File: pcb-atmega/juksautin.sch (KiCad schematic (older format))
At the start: 29 parts, among them J1 Screw_Terminal_01x09, J3 USB_C_Receptacle_USB2.0, J4 TagConnect, U1 SP3485EN, U2 SRV05-4, U3 LM2576S-5, U4 ATmega32U4-AU, Y1 X322516MLB4SI

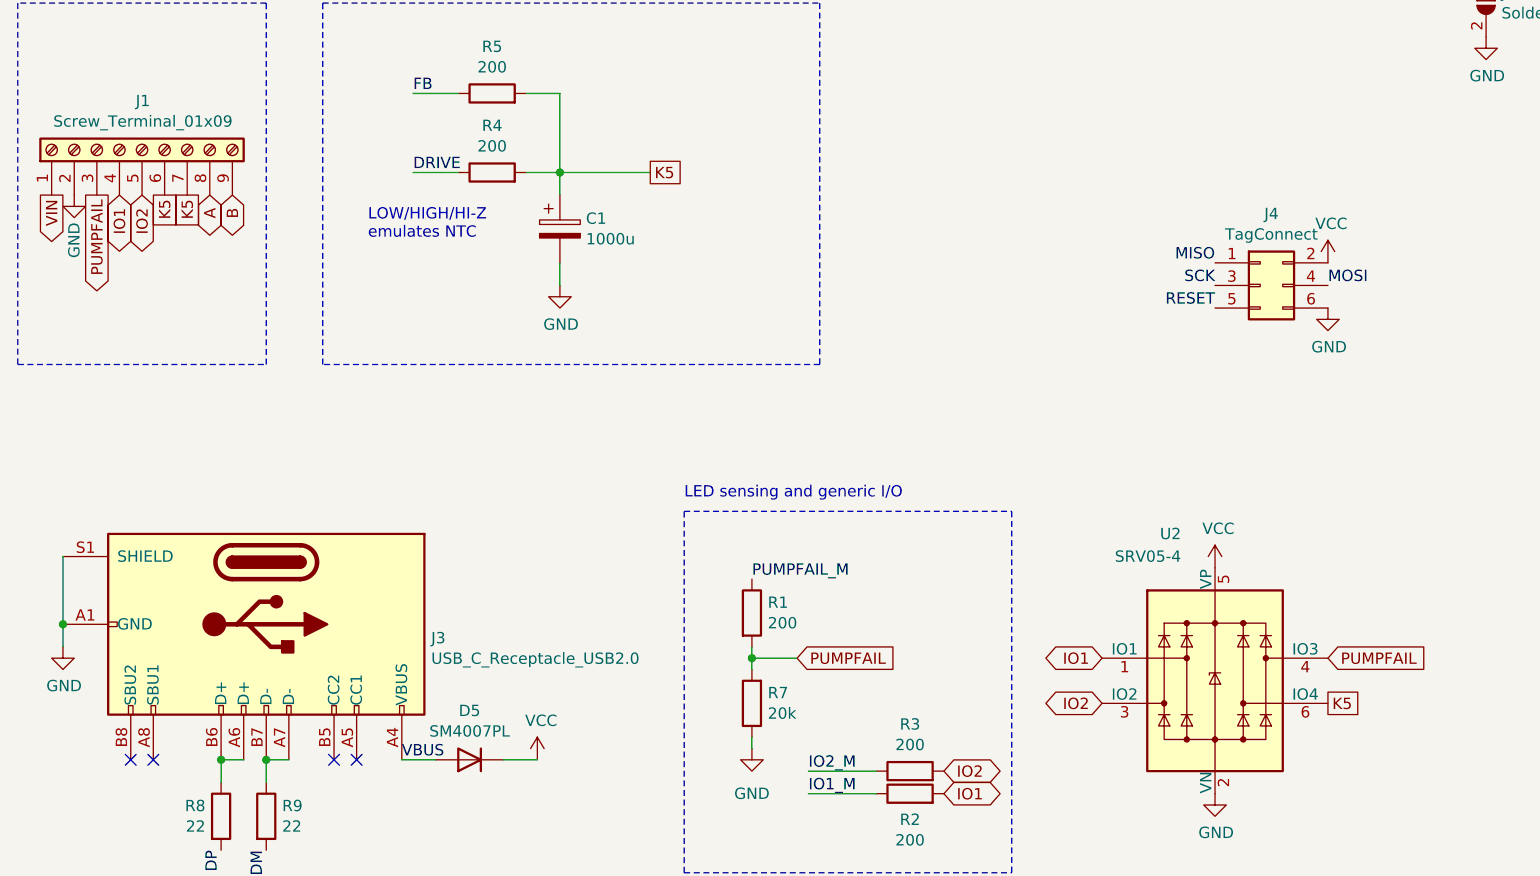
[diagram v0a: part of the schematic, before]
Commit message: pcb: Rename K5 to K9 everywhere
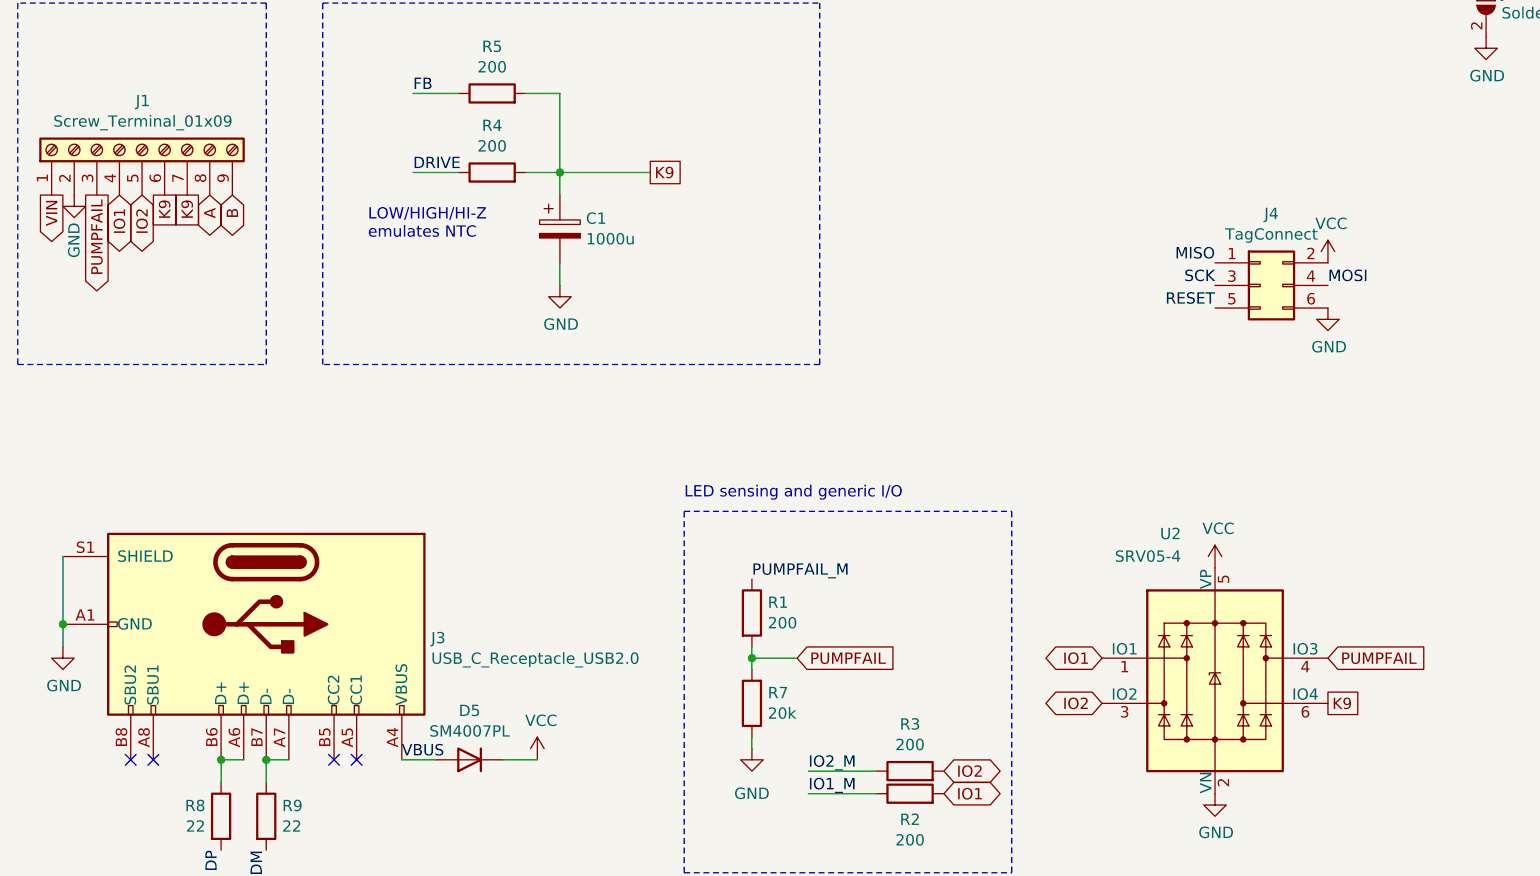
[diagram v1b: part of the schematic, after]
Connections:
- net labels added: K9
- net labels removed: K5
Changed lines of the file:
@@
 $EndComp
 Text GLabel 3650 3800 2    50   UnSpc ~ 0
-K5
+K9
 $Comp
 L Device:R R4
@@
 B
 Text GLabel 1600 3900 3    50   UnSpc ~ 0
-K5
+K9
 Text GLabel 1500 3900 3    50   UnSpc ~ 0
-K5
+K9
 Text GLabel 5150 1750 2    50   3State ~ 0
 A
@@
 PUMPFAIL
 Text GLabel 6650 6150 2    50   UnSpc ~ 0
-K5
+K9
 $Comp
 L power:GND #PWR011

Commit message: pcb: Route everything Atmega board
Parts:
- removed TP1: AR, TestPoint:TestPoint_Pad_D1.0mm, symbol Connector:TestPoint
- added J2: Power out, Connector_PinHeader_2.54mm:PinHeader_1x02_P2.54mm_Vertical, symbol Connector:Conn_01x02_Male
- added J5: Conn_01x03, Connector_PinHeader_2.54mm:PinHeader_1x03_P2.54mm_Vertical, symbol Connector_Generic:Conn_01x03
- added J6: AREF_OUT, Connector_PinHeader_2.54mm:PinHeader_1x02_P2.54mm_Vertical, symbol Connector_Generic:Conn_01x02
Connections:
- wire segments 71 -> 79
- no-connect marks 19 -> 16
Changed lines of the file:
@@
 Wire Wire Line
 	9450 1000 9450 1100
-Wire Wire Line
-	9450 1100 9550 1100
-Connection ~ 9550 1100
-Wire Wire Line
-	9550 1100 9650 1100
 Text Label 8950 2000 2    50   ~ 0
 AREF
@@
 Text GLabel 5650 6150 0    50   3State ~ 0
 IO2
-Text GLabel 6650 5950 2    50   Input ~ 0
+Text GLabel 6650 6150 2    50   Input ~ 0
 PUMPFAIL
-Text GLabel 6650 6150 2    50   UnSpc ~ 0
+Text GLabel 6650 5950 2    50   UnSpc ~ 0
 K9
 $Comp
@@
 Wire Wire Line
 	4100 6300 4100 6350
-Connection ~ 9450 4700
-Connection ~ 9450 1100
-$Comp
-L MCU_Microchip_ATmega:ATmega32U4-AU U4
-U 1 1 60B53808
-P 9550 2900
-F 0 "U4" H 9550 1011 50  0000 L CNN
-F 1 "ATmega32U4-AU" H 9550 920 50  0000 L CNN
-F 2 "Package_QFP:TQFP-44_10x10mm_P0.8mm" H 9550 2900 50  0001 C CIN
-F 3 "http://ww1.microchip.com/downloads/en/DeviceDoc/Atmel-7766-8-bit-AVR-ATmega16U4-32U4_Datasheet.pdf" H 9550 2900 50  0001 C CNN
-F 4 "C44854" H 9550 2900 50  0001 C CNN "LCSC"
-	1    9550 2900
-	1    0    0    -1
-$EndComp
 Text GLabel 4950 6450 2    50   3State ~ 0
 IO2
@@
 NoConn ~ 10150 2400
 NoConn ~ 10150 2600
-NoConn ~ 10150 3000
-NoConn ~ 10150 3100
-NoConn ~ 10150 3200
-NoConn ~ 10150 3300
 NoConn ~ 10150 3500
 NoConn ~ 10150 3600
 NoConn ~ 10150 3800
 NoConn ~ 10150 3900
-Connection ~ 8400 2000
-$Comp
-L Connector:TestPoint TP1
-U 1 1 60EAECA1
-P 8400 2000
-F 0 "TP1" V 8446 2188 50  0000 L CNN
-F 1 "AR" V 8355 2188 50  0000 L CNN
-F 2 "TestPoint:TestPoint_Pad_D1.0mm" H 8600 2000 50  0001 C CNN
-F 3 "~" H 8600 2000 50  0001 C CNN
-	1    8400 2000
-	0    -1   -1   0
-$EndComp
 Text Label 8950 1400 2    50   ~ 0
 RESET
@@
 	1    0    0    -1
 $EndComp
+$Comp
+L power:GND #PWR0106
+U 1 1 60C3103F
+P 5800 3500
+F 0 "#PWR0106" H 5800 3250 50  0001 C CNN
+F 1 "GND" H 5950 3500 50  0000 C CNN
+F 2 "" H 5800 3500 50  0001 C CNN
+F 3 "" H 5800 3500 50  0001 C CNN
+	1    5800 3500
+	1    0    0    -1
+$EndComp
+$Comp
+L power:VCC #PWR0110
+U 1 1 60C31968
+P 5800 3400
+F 0 "#PWR0110" H 5800 3250 50  0001 C CNN
+F 1 "VCC" H 5950 3400 50  0000 C CNN
+F 2 "" H 5800 3400 50  0001 C CNN
+F 3 "" H 5800 3400 50  0001 C CNN
+	1    5800 3400
+	1    0    0    -1
+$EndComp
+$Comp
+L Connector:Conn_01x02_Male J2
+U 1 1 60C5E35B
+P 5600 3400
+F 0 "J2" H 5708 3581 50  0000 R CNN
+F 1 "Power out" H 5708 3490 50  0000 R CNN
+F 2 "Connector_PinHeader_2.54mm:PinHeader_1x02_P2.54mm_Vertical" H 5600 3400 50  0001 C CNN
+F 3 "~" H 5600 3400 50  0001 C CNN
+	1    5600 3400
+	1    0    0    -1
+$EndComp
+Connection ~ 9450 4700
+Connection ~ 9450 1100
+Wire Wire Line
+	9550 1100 9650 1100
+Wire Wire Line
+	9450 1100 9550 1100
+Connection ~ 9550 1100
+$Comp
+L MCU_Microchip_ATmega:ATmega32U4-AU U4
+U 1 1 60B53808
+P 9550 2900
+F 0 "U4" H 9550 1011 50  0000 L CNN
+F 1 "ATmega32U4-AU" H 9550 920 50  0000 L CNN
+F 2 "Package_QFP:TQFP-44_10x10mm_P0.8mm" H 9550 2900 50  0001 C CIN
+F 3 "http://ww1.microchip.com/downloads/en/DeviceDoc/Atmel-7766-8-bit-AVR-ATmega16U4-32U4_Datasheet.pdf" H 9550 2900 50  0001 C CNN
+F 4 "C44854" H 9550 2900 50  0001 C CNN "LCSC"
+	1    9550 2900
+	1    0    0    -1
+$EndComp
+$Comp
+L Connector_Generic:Conn_01x03 J5
+U 1 1 60C825FD
+P 10500 3200
+F 0 "J5" H 10580 3242 50  0000 L CNN
+F 1 "Conn_01x03" H 10580 3151 50  0000 L CNN
+F 2 "Connector_PinHeader_2.54mm:PinHeader_1x03_P2.54mm_Vertical" H 10500 3200 50  0001 C CNN
+F 3 "~" H 10500 3200 50  0001 C CNN
+	1    10500 3200
+	1    0    0    -1
+$EndComp
+NoConn ~ 10150 3100
+Wire Wire Line
+	10300 3300 10150 3300
+Wire Wire Line
+	10150 3200 10300 3200
+Wire Wire Line
+	10150 3000 10300 3000
+Wire Wire Line
+	10300 3000 10300 3100
+$Comp
+L Connector_Generic:Conn_01x02 J6
+U 1 1 60CB591E
+P 7900 2150
+F 0 "J6" H 7818 2367 50  0000 C CNN
+F 1 "AREF_OUT" H 7818 2276 50  0000 C CNN
+F 2 "Connector_PinHeader_2.54mm:PinHeader_1x02_P2.54mm_Vertical" H 7900 2150 50  0001 C CNN
+F 3 "~" H 7900 2150 50  0001 C CNN
+	1    7900 2150
+	-1   0    0    -1
+$EndComp
+Wire Wire Line
+	8100 2250 8400 2250
+Connection ~ 8400 2250
+Wire Wire Line
+	8100 2150 8250 2150
+Wire Wire Line
+	8250 2150 8250 2000
+Wire Wire Line
+	8250 2000 8400 2000
+Connection ~ 8400 2000
 $EndSCHEMATC

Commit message: pcb: Make schema a bit more readable
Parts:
- J5: value Conn_01x03 -> EXTRA
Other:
- moved on the sheet: C2, C3
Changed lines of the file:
@@
 L power:GND #PWR0109
 U 1 1 60A206FA
-P 2100 2250
-F 0 "#PWR0109" H 2100 2000 50  0001 C CNN
-F 1 "GND" H 2105 2077 50  0000 C CNN
-F 2 "" H 2100 2250 50  0001 C CNN
-F 3 "" H 2100 2250 50  0001 C CNN
-	1    2100 2250
+P 2100 2300
+F 0 "#PWR0109" H 2100 2050 50  0001 C CNN
+F 1 "GND" H 2105 2127 50  0000 C CNN
+F 2 "" H 2100 2300 50  0001 C CNN
+F 3 "" H 2100 2300 50  0001 C CNN
+	1    2100 2300
 	1    0    0    -1
 $EndComp
@@
 Text GLabel 1000 3900 3    50   Output ~ 0
 VIN
-Text GLabel 1150 1650 0    50   Input ~ 0
+Text GLabel 1150 1600 0    50   Input ~ 0
 VIN
 Text Notes 3800 5250 0    50   ~ 0
@@
 	1    0    0    -1
 $EndComp
-Text Label 4250 1650 0    50   ~ 0
+Text Label 4050 1650 0    50   ~ 0
 RX
 Wire Wire Line
-	4250 1650 4350 1650
-Text Label 4250 2050 0    50   ~ 0
+	4050 1650 4350 1650
+Text Label 4050 2050 0    50   ~ 0
 TX
 Wire Wire Line
-	4250 2050 4350 2050
+	4050 2050 4350 2050
 Text Label 10150 2800 0    50   ~ 0
 RX
@@
 L Regulator_Switching:LM2576S-5 U3
 U 1 1 60F0FB4A
-P 2100 1750
-F 0 "U3" H 2100 2117 50  0000 C CNN
-F 1 "LM2576S-5" H 2100 2026 50  0000 C CNN
-F 2 "Package_TO_SOT_SMD:TO-263-5_TabPin3" H 2100 1500 50  0001 L CIN
-F 3 "http://www.ti.com/lit/ds/symlink/lm2576.pdf" H 2100 1750 50  0001 C CNN
-F 4 "C10002" H 2100 1750 50  0001 C CNN "LCSC"
-	1    2100 1750
+P 2100 1700
+F 0 "U3" H 2100 2067 50  0000 C CNN
+F 1 "LM2576S-5" H 2100 1976 50  0000 C CNN
+F 2 "Package_TO_SOT_SMD:TO-263-5_TabPin3" H 2100 1450 50  0001 L CIN
+F 3 "http://www.ti.com/lit/ds/symlink/lm2576.pdf" H 2100 1700 50  0001 C CNN
+F 4 "C10002" H 2100 1700 50  0001 C CNN "LCSC"
+	1    2100 1700
 	1    0    0    -1
 $EndComp
@@
 $EndComp
 Wire Wire Line
-	1250 2250 1250 2050
-Wire Wire Line
-	1600 1850 1600 2250
-Wire Wire Line
-	1600 2250 1250 2250
-Wire Wire Line
-	1600 2250 2100 2250
-Connection ~ 1600 2250
-Wire Wire Line
-	2100 2050 2100 2250
-Connection ~ 2100 2250
-Wire Wire Line
-	2100 2250 2650 2250
-Wire Wire Line
-	3150 1600 3150 1850
+	1250 2300 1250 2100
+Wire Wire Line
+	1600 2300 1250 2300
+Wire Wire Line
+	1600 2300 2100 2300
+Connection ~ 1600 2300
+Connection ~ 2100 2300
+Wire Wire Line
+	3150 1600 3150 1900
 Connection ~ 3150 1600
 $Comp
 L Device:L L1
 U 1 1 60F8C9F3
-P 2900 1850
-F 0 "L1" V 3090 1850 50  0000 C CNN
-F 1 "100uH" V 2999 1850 50  0000 C CNN
-F 2 "Inductor_SMD:L_0805_2012Metric" H 2900 1850 50  0001 C CNN
-F 3 "~" H 2900 1850 50  0001 C CNN
-F 4 "C68035" V 2900 1850 50  0001 C CNN "LCSC"
-	1    2900 1850
+P 2900 1900
+F 0 "L1" V 3090 1900 50  0000 C CNN
+F 1 "100uH" V 2999 1900 50  0000 C CNN
+F 2 "Inductor_SMD:L_0805_2012Metric" H 2900 1900 50  0001 C CNN
+F 3 "~" H 2900 1900 50  0001 C CNN
+F 4 "C68035" V 2900 1900 50  0001 C CNN "LCSC"
+	1    2900 1900
 	0    -1   -1   0
 $EndComp
-Wire Wire Line
-	3050 1850 3150 1850
 $Comp
 L Diode:1N5822 D1
 U 1 1 60F94C7F
-P 2650 2050
-F 0 "D1" V 2604 2130 50  0000 L CNN
-F 1 "SS34" V 2695 2130 50  0000 L CNN
-F 2 "Diode_SMD:D_SMA" H 2650 1875 50  0001 C CNN
-F 3 "http://www.vishay.com/docs/88526/1n5820.pdf" H 2650 2050 50  0001 C CNN
-F 4 "C8678" V 2650 2050 50  0001 C CNN "LCSC"
-	1    2650 2050
+P 2650 2100
+F 0 "D1" V 2604 2180 50  0000 L CNN
+F 1 "SS34" V 2695 2180 50  0000 L CNN
+F 2 "Diode_SMD:D_SMA" H 2650 1925 50  0001 C CNN
+F 3 "http://www.vishay.com/docs/88526/1n5820.pdf" H 2650 2100 50  0001 C CNN
+F 4 "C8678" V 2650 2100 50  0001 C CNN "LCSC"
+	1    2650 2100
 	0    1    1    0
 $EndComp
 Wire Wire Line
-	1150 1650 1250 1650
+	1150 1600 1250 1600
 $Comp
 L Device:CP C2
 U 1 1 60F96B50
-P 1250 1900
-F 0 "C2" H 1368 1946 50  0000 L CNN
-F 1 "100u" H 1368 1855 50  0000 L CNN
-F 2 "Capacitor_SMD:CP_Elec_6.3x7.7" H 1288 1750 50  0001 C CNN
-F 3 "~" H 1250 1900 50  0001 C CNN
-F 4 "C99837" H 1250 1900 50  0001 C CNN "LCSC"
-	1    1250 1900
-	1    0    0    -1
-$EndComp
-Wire Wire Line
-	1250 1750 1250 1650
-Connection ~ 1250 1650
-Wire Wire Line
-	1250 1650 1600 1650
-Wire Wire Line
-	2600 1650 2600 1600
+P 1250 1950
+F 0 "C2" H 1368 1996 50  0000 L CNN
+F 1 "100u" H 1368 1905 50  0000 L CNN
+F 2 "Capacitor_SMD:CP_Elec_6.3x7.7" H 1288 1800 50  0001 C CNN
+F 3 "~" H 1250 1950 50  0001 C CNN
+F 4 "C99837" H 1250 1950 50  0001 C CNN "LCSC"
+	1    1250 1950
+	1    0    0    -1
+$EndComp
+Wire Wire Line
+	1250 1800 1250 1600
+Connection ~ 1250 1600
+Wire Wire Line
+	1250 1600 1600 1600
 Wire Notes Line
 	850  1000 3650 1000
 Wire Notes Line
 	3650 1000 3650 2600
-Connection ~ 3150 1850
 $Comp
 L Device:CP C3
 U 1 1 60F97AAC
-P 3150 2050
-F 0 "C3" H 3268 2096 50  0000 L CNN
-F 1 "1000u" H 3268 2005 50  0000 L CNN
-F 2 "Capacitor_SMD:CP_Elec_8x10" H 3188 1900 50  0001 C CNN
-F 3 "~" H 3150 2050 50  0001 C CNN
-F 4 "C134755" H 3150 2050 50  0001 C CNN "LCSC"
-	1    3150 2050
-	1    0    0    -1
-$EndComp
-Wire Wire Line
-	2600 1850 2650 1850
-Wire Wire Line
-	2650 1850 2650 1900
-Connection ~ 2650 1850
-Wire Wire Line
-	2650 1850 2750 1850
-Wire Wire Line
-	2650 2200 2650 2250
-Wire Wire Line
-	2650 2250 3150 2250
-Connection ~ 2650 2250
-Wire Wire Line
-	3150 1850 3150 1900
-Wire Wire Line
-	3150 2200 3150 2250
+P 3150 2100
+F 0 "C3" H 3268 2146 50  0000 L CNN
+F 1 "1000u" H 3268 2055 50  0000 L CNN
+F 2 "Capacitor_SMD:CP_Elec_8x10" H 3188 1950 50  0001 C CNN
+F 3 "~" H 3150 2100 50  0001 C CNN
+F 4 "C134755" H 3150 2100 50  0001 C CNN "LCSC"
+	1    3150 2100
+	1    0    0    -1
+$EndComp
 Wire Notes Line
 	850  2600 3650 2600
@@
 P 10500 3200
 F 0 "J5" H 10580 3242 50  0000 L CNN
-F 1 "Conn_01x03" H 10580 3151 50  0000 L CNN
+F 1 "EXTRA" H 10580 3151 50  0000 L CNN
 F 2 "Connector_PinHeader_2.54mm:PinHeader_1x03_P2.54mm_Vertical" H 10500 3200 50  0001 C CNN
 F 3 "~" H 10500 3200 50  0001 C CNN
@@
 	8250 2000 8400 2000
 Connection ~ 8400 2000
+Wire Wire Line
+	2600 1800 2650 1800
+Wire Wire Line
+	2650 1800 2650 1900
+Wire Wire Line
+	1600 1800 1600 2300
+Wire Wire Line
+	2100 2000 2100 2300
+Wire Wire Line
+	2750 1900 2650 1900
+Connection ~ 2650 1900
+Wire Wire Line
+	2650 1900 2650 1950
+Wire Wire Line
+	3050 1900 3150 1900
+Connection ~ 3150 1900
+Wire Wire Line
+	3150 1900 3150 1950
+Wire Wire Line
+	3150 2250 3150 2300
+Wire Wire Line
+	3150 2300 2650 2300
+Wire Wire Line
+	2650 2300 2650 2250
+Wire Wire Line
+	2650 2300 2100 2300
+Connection ~ 2650 2300
 $EndSCHEMATC

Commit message: pcb: Replace LM2576 with Recom R-78E5.0 THT DC/DC converter
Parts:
- removed C2: 100u, Capacitor_SMD:CP_Elec_6.3x7.7, symbol Device:CP
- removed C3: 1000u, Capacitor_SMD:CP_Elec_8x10, symbol Device:CP
- removed D1: SS34, Diode_SMD:D_SMA, symbol Diode:1N5822
- removed L1: 100uH, Inductor_SMD:L_0805_2012Metric, symbol Device:L
- removed U3: LM2576S-5, Package_TO_SOT_SMD:TO-263-5_TabPin3, symbol Regulator_Switching:LM2576S-5
- added C2: 10u, Capacitor_SMD:C_0402_1005Metric, symbol Device:C
- added C3: 10u, Capacitor_SMD:C_1206_3216Metric, symbol Device:C
- added U3: R-78E5.0-0.5, Converter_DCDC:Converter_DCDC_RECOM_R-78E-0.5_THT, symbol Regulator_Switching:R-78E5.0-0.5
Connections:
- wire segments 79 -> 68
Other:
- moved on the sheet: U1
